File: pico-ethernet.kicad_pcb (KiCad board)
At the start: 2 copper layers, 55 x 22 mm, 29 parts, among them J1 Conn_01x20_Pin, J2 Conn_01x02_Pin, J3 VR05S05, J4 SI-52003-F, J5 Conn_01x02, U1 ENC28J60x-SS, Y1 25MHz

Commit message: tweaks
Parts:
- moved C9 1.83 mm to (141.7, 127.8), turned to -90 degrees
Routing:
- net Net-(U1-VCAP): track 3.46 -> 5.32 mm
- net Net-(J4-RD-): track 51.7 -> 52.4 mm

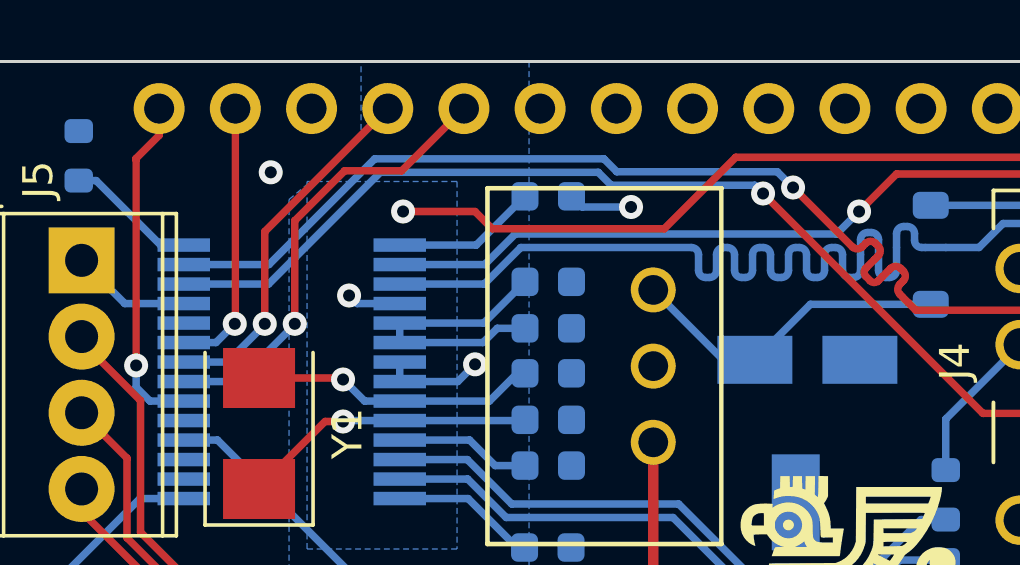
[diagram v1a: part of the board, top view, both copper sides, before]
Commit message: connect reset
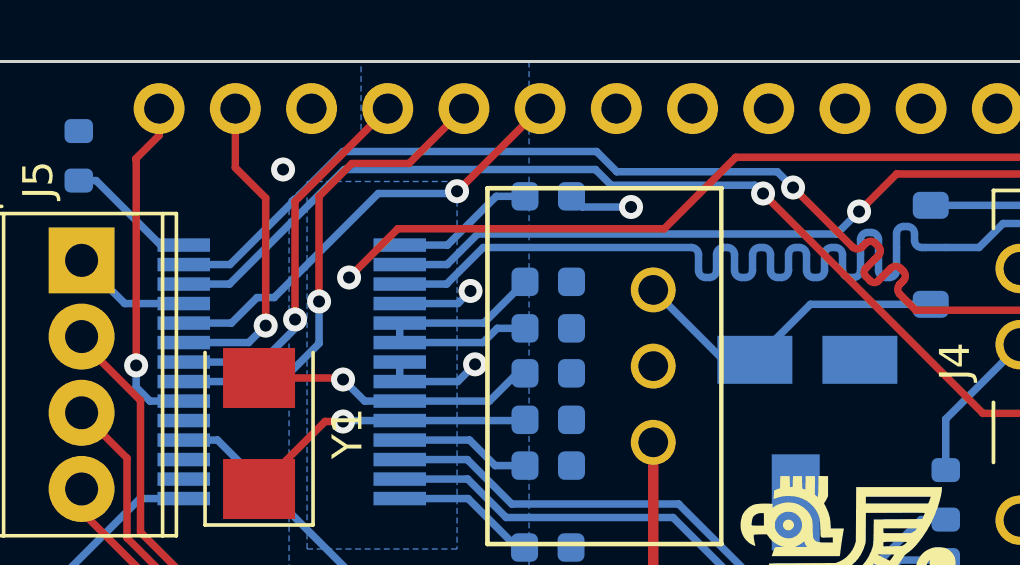
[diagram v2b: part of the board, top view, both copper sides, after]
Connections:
- J1 pad 15: unconnected-(J1-Pin_15-Pad15) -> Net-(J1-Pin_15)
- U1 pad 10: unconnected-(U1-~{RESET}-Pad10) -> Net-(J1-Pin_15)
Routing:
- net Net-(J1-Pin_15): track 0.00 -> 14.8 mm, vias 0 -> 1
- net +3.3V: track 68.9 -> 71.1 mm
- net Net-(J1-Pin_19): track 9.14 -> 10.6 mm
- net Net-(J1-Pin_16): track 15.1 -> 16.0 mm
- net GND: track 11.5 -> 12.2 mm
- net Net-(J1-Pin_17): track 12.1 -> 12.8 mm

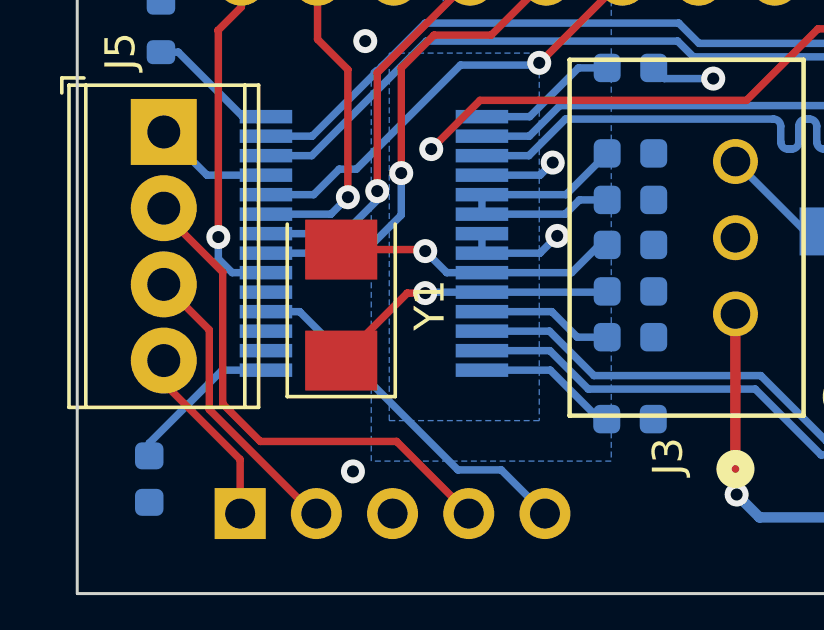
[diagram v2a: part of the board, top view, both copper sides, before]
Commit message: move oscillator away from vias
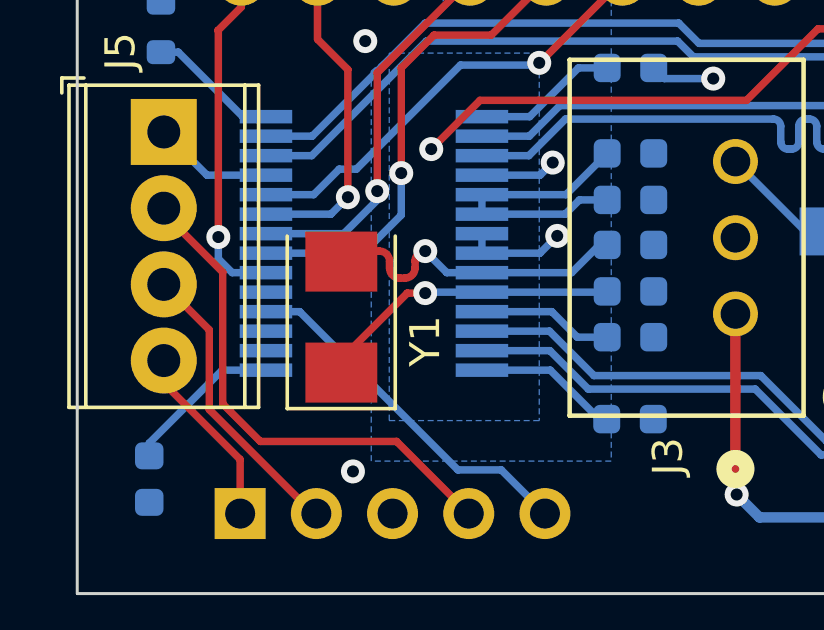
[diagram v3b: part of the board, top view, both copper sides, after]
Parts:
- moved Y1 0.40 mm to (148.1, 122.4)
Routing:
- net Net-(U1-OSC1): track 9.66 -> 10.9 mm
- net Net-(U1-OSC2): track 11.0 -> 11.6 mm
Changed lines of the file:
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@@
 	(footprint "Crystal:Crystal_SMD_5032-2Pin_5.0x3.2mm"
 		(layer "F.Cu")
-		(at 148.11 121.956 90)
+		(at 148.11 122.356 90)
 		(descr "SMD Crystal SERIES SMD2520/2 http://www.icbase.com/File/PDF/HKC/HKC00061008.pdf, 5.0x3.2mm^2 package")
 		(tags "SMD SMT crystal")
 		(property "Reference" "Y1"
-			(at 0 2.95 90)
+			(at -0.8 2.8 90)
 			(layer "F.SilkS")
 			(effects
@@
 			)
 		)
-		(sheetname "Root")
-		(sheetfile "pico-ethernet.kicad_sch")
 		(attr through_hole)
 		(fp_line
@@
 		(fp_arc
 			(start 8.375 6.675)
-			(mid 8.395283 6.484922)
+			(mid 8.395272 6.484918)
 			(end 8.5 6.325)
 			(stroke
@@
 		(fp_arc
 			(start 8.99 8.2)
-			(mid 8.664251 7.44486)
+			(mid 8.66425 7.44486)
 			(end 8.375 6.675)
 			(stroke
@@
 		(fp_arc
 			(start 8.99 8.2)
-			(mid 8.994769 10.775349)
+			(mid 8.994768 10.775349)
 			(end 8.2 13.225)
 			(stroke
@@
 	)
 	(segment
-		(start 148.11 120.106)
-		(end 150.86 120.106)
+		(start 148.46 120.156)
+		(end 148.11 120.506)
 		(width 0.25)
 		(layer "F.Cu")
@@
 	)
 	(segment
-		(start 150.86 120.106)
-		(end 150.91 120.156)
+		(start 149.21 120.156)
+		(end 149.11 120.156)
+		(width 0.25)
+		(layer "F.Cu")
+		(net 4)
+	)
+	(segment
+		(start 149.72 120.716)
+		(end 149.72 120.496)
+		(width 0.25)
+		(layer "F.Cu")
+		(net 4)
+	)
+	(segment
+		(start 150.57 120.496)
+		(end 150.57 120.716)
+		(width 0.25)
+		(layer "F.Cu")
+		(net 4)
+	)
+	(segment
+		(start 149.11 120.156)
+		(end 148.46 120.156)
+		(width 0.25)
+		(layer "F.Cu")
+		(net 4)
+	)
+	(segment
+		(start 150.23 121.056)
+		(end 150.06 121.056)
+		(width 0.25)
+		(layer "F.Cu")
+		(net 4)
+	)
+	(segment
+		(start 149.38 120.156)
+		(end 149.21 120.156)
 		(width 0.25)
 		(layer "F.Cu")
@@
 		(net 4)
 	)
+	(arc
+		(start 150.06 121.056)
+		(mid 149.819584 120.956416)
+		(end 149.72 120.716)
+		(width 0.25)
+		(layer "F.Cu")
+		(net 4)
+	)
+	(arc
+		(start 149.72 120.496)
+		(mid 149.620416 120.255584)
+		(end 149.38 120.156)
+		(width 0.25)
+		(layer "F.Cu")
+		(net 4)
+	)
+	(arc
+		(start 150.57 120.716)
+		(mid 150.470416 120.956416)
+		(end 150.23 121.056)
+		(width 0.25)
+		(layer "F.Cu")
+		(net 4)
+	)
+	(arc
+		(start 150.91 120.156)
+		(mid 150.669584 120.255584)
+		(end 150.57 120.496)
+		(width 0.25)
+		(layer "F.Cu")
+		(net 4)
+	)
 	(segment
 		(start 152.8 120.875)
@@
 	)
 	(segment
+		(start 148.71 123.956)
+		(end 148.71 124.1)
+		(width 0.25)
+		(layer "F.Cu")
+		(net 5)
+	)
+	(segment
 		(start 150.31 121.556)
 		(end 150.91 121.556)
@@
 	)
 	(segment
-		(start 148.71 123.956)
-		(end 148.71 124.1)
+		(start 149.06 123.806)
+		(end 148.51 123.806)
 		(width 0.25)
 		(layer "F.Cu")
@@
 	)
 	(segment
-		(start 149.06 123.806)
-		(end 148.11 123.806)
+		(start 148.51 123.806)
+		(end 148.11 124.206)
 		(width 0.25)
 		(layer "F.Cu")
@@
 	)
 	(segment
-		(start 148.11 123.806)
+		(start 148.11 124.206)
 		(end 148.11 123.756)
 		(width 0.25)
@@
 	)
 	(generated
+		(type tuning_pattern)
+		(name "Tuning Pattern")
+		(layer "F.Cu")
+		(base_line
+			(pts
+				(xy 150.91 120.156) (xy 149.11 120.156)
+			)
+		)
+		(corner_radius_percent 80)
+		(end
+			(xy 149.11 120.156)
+		)
+		(initial_side "left")
+		(last_diff_pair_gap 0.18)
+		(last_netname "Net-(U1-OSC1)")
+		(last_status "too_short")
+		(last_track_width 0.25)
+		(last_tuning "7.7991 mm (too short)")
+		(max_amplitude 1)
+		(min_amplitude 0.2)
+		(min_spacing 0.85)
+		(origin
+			(xy 150.91 120.156)
+		)
+		(override_custom_rules no)
+		(rounded yes)
+		(single_sided no)
+		(target_length 1000000)
+		(target_length_max 1000000.1)
+		(target_length_min 999999.9)
+		(target_skew 0)
+		(target_skew_max 0.1)
+		(target_skew_min -0.1)
+		(tuning_mode "single")
+		(members 2bec640e-f81f-4cb3-93f1-2ea21976ad1d 4d3c1477-a58f-4e86-bf67-79c8f66cdaa2
+			4d699b47-22d5-4b32-ab03-c4b0528399f2 52d23372-d02a-4210-bf84-d35afd700b88
+			99d88278-f4b5-4c0a-a3f3-d991cf100211 abd21ed7-93aa-4310-a342-33e07486fda1
+			bfa728bd-7933-4952-a0ac-2fc37193387b d1e1ab7e-0331-4dc3-b660-3bccf7936e9f
+			de165d64-ebcc-4552-8e6b-5817b278b23f
+		)
+	)
+	(generated

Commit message: v1
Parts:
- moved C7 3.44 mm to (191.9, 119.2), turned to 90 degrees
- moved C3 0.40 mm to (157.7, 126.2)
- moved R3 0.39 mm to (191.9, 122.4)
- moved C8 0.35 mm to (188.3, 122.4)
- moved C10 0.33 mm to (157.8, 123.4)
- moved R2 0.31 mm to (190.3, 122.4)
- moved FB1 0.23 mm to (186.7, 122.4)
- moved C6 0.21 mm to (157.8, 121.7)
- moved C4 0.14 mm to (157.7, 116.8)
- moved R4 0.12 mm to (185.0, 122.4)
- moved C5 0.11 mm to (157.8, 120.1)
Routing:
- net +24V: track 24.0 -> 22.8 mm
- net Net-(U1-OSC2): track 11.6 -> 10.5 mm
